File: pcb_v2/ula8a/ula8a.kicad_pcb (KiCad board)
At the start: 2 copper layers, 126.3 x 210 mm, 81 parts, among them J1 designador, J2 operador, J3 operador, J4 operador, J5 operador, J6 operador, J7 operador, J8 bus_mgrf_1, J9 bus_mgrf_2, Q1 BC548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

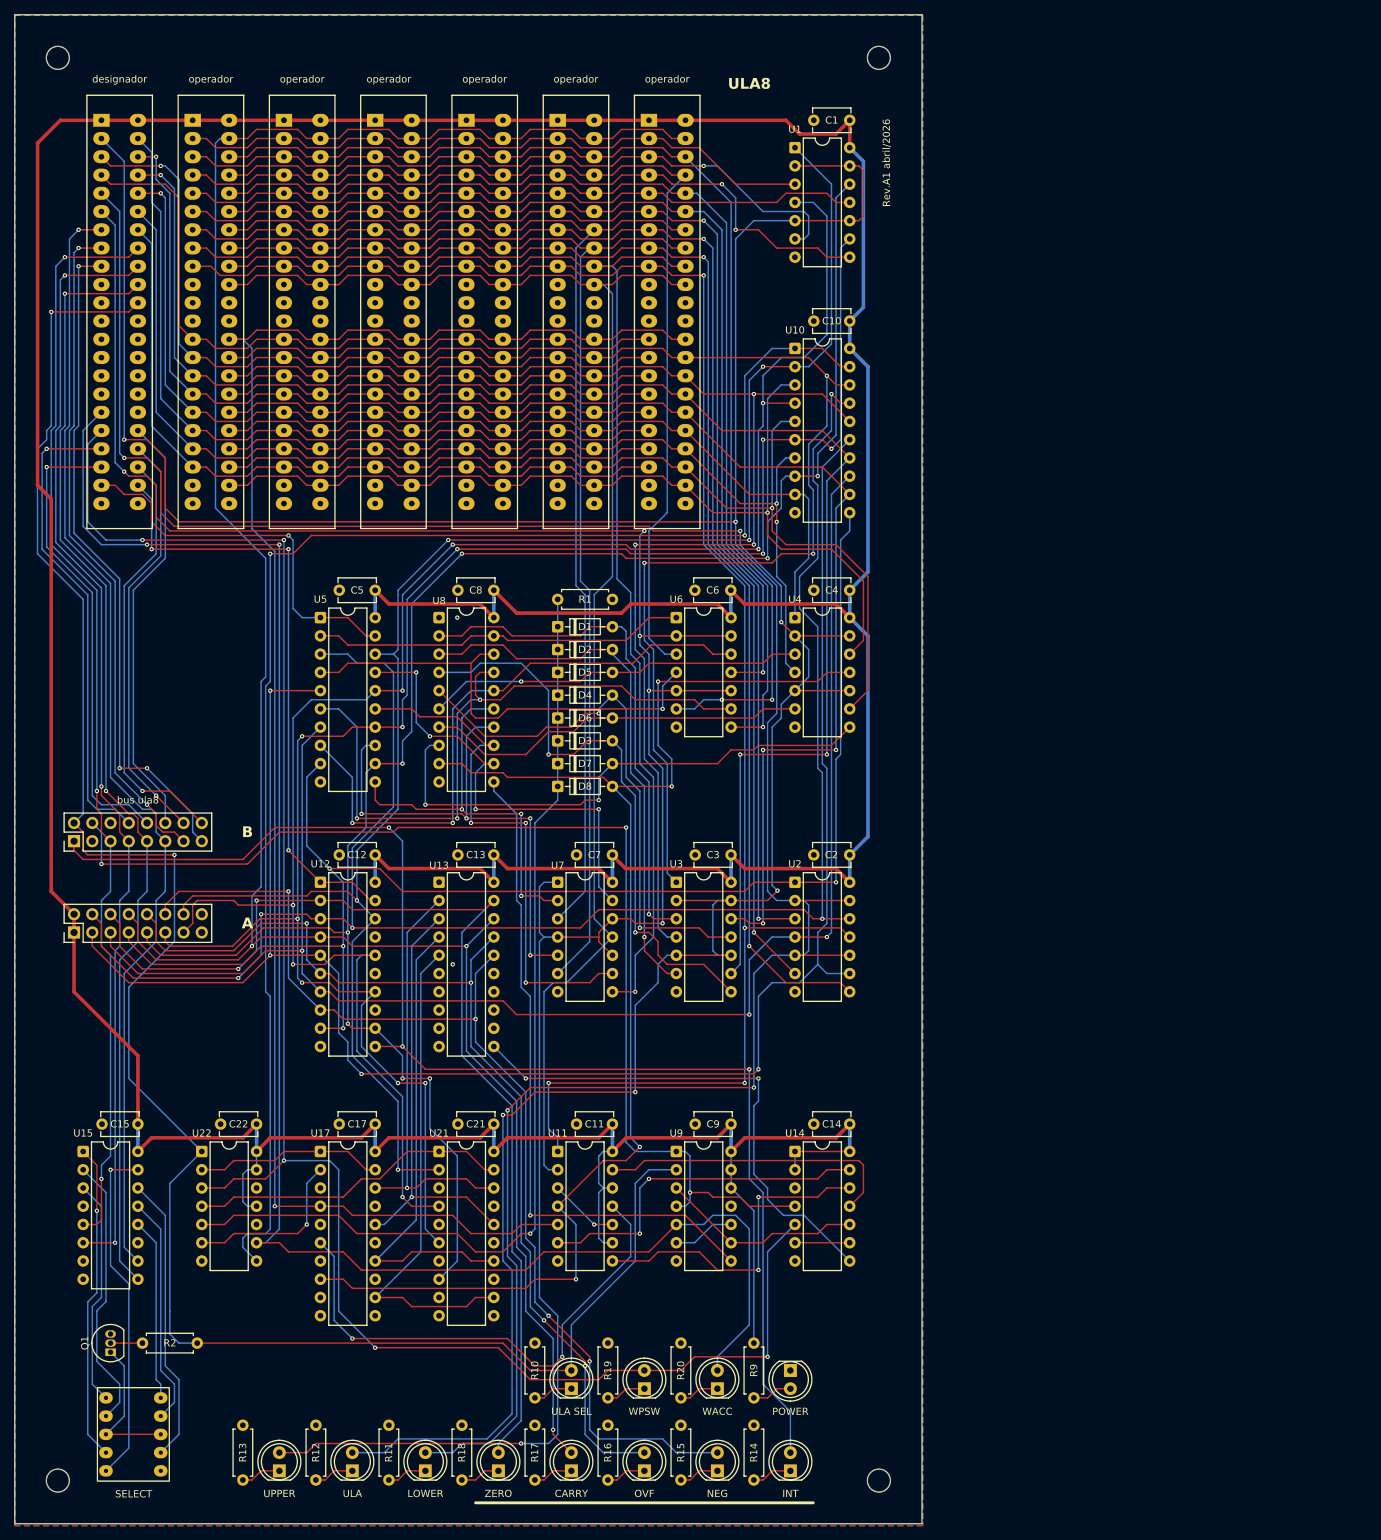
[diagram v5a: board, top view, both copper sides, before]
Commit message: atualização do conector flat
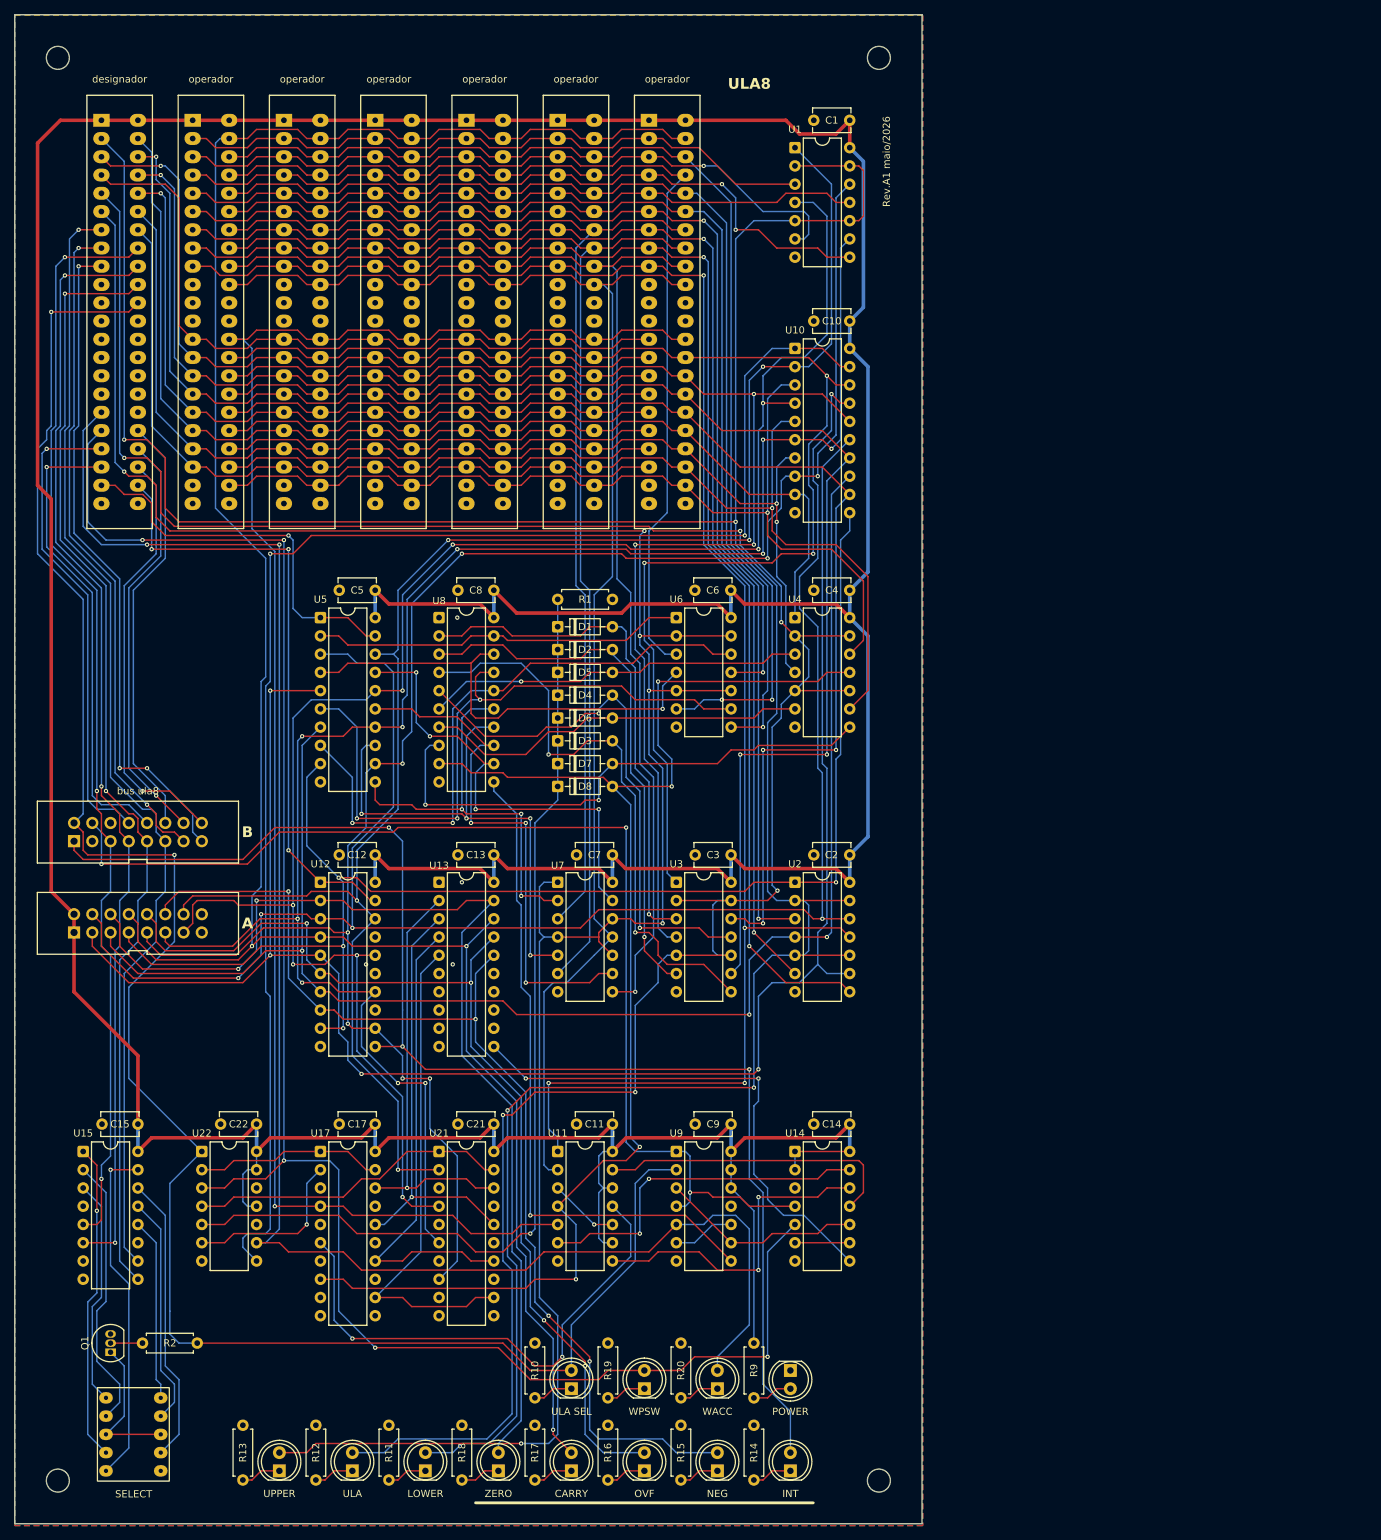
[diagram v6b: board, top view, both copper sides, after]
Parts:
- J8, J9: footprint Connector_PinHeader_2.54mm:PinHeader_2x08_P2.54mm_Vertical -> edge_connector:conector 02x08
- moved J8 8.98 mm to (30.5, 139.7), turned to 0 degrees
- moved J9 8.98 mm to (30.5, 127.0), turned to 0 degrees
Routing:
- net data_1: track 253.8 -> 251.6 mm, vias 7 -> 8
- net data_4: track 200.9 -> 199.1 mm
- net GND: vias 2 -> 4
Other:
- board text added: "Rev.A1 maio/2026"
- board text removed: "Rev.A1 abril/2026"
